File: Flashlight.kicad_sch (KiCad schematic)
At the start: 11 parts

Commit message: Finalized Kicad PCB Design
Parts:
- removed BT1: Battery_Cell, symbol Device:Battery_Cell
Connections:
- net 5V renamed 12V2
- net 12V2: no longer D1.2 (A), D10.2 (A), D7.2 (A), D8.2 (A), D9.2 (A)
- new net 12V1: D1.2 (A)
- new net 12V3: D10.2 (A), D7.2 (A), D8.2 (A), D9.2 (A)
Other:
- moved on the sheet: D1, D10, D2, D3, D4, D5, D6, D7, D8, D9

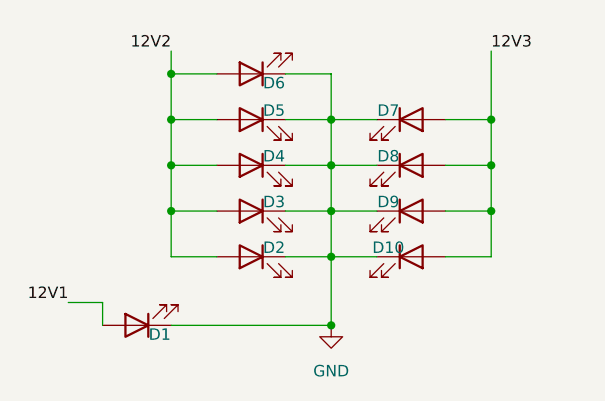
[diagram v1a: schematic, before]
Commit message: Made the PCB one Sided
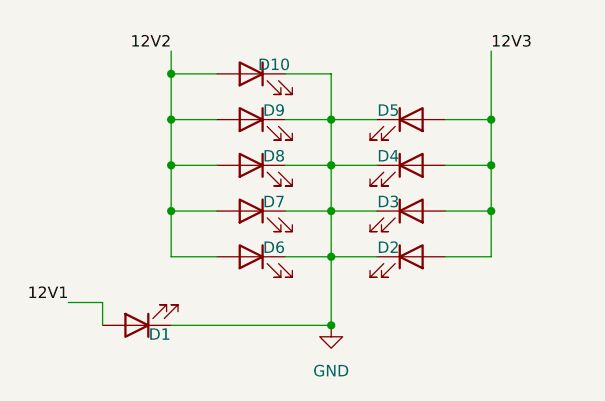
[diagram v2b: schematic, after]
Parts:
- renumbered D5 to D2, D6 to D3, D8 to D4, D7 to D5, D2 to D6, D3 to D7, D4 to D8
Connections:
- net 12V2: now also D10.2 (A), D9.2 (A); no longer D2.2 (A), D3.2 (A)
- net 12V3: now also D2.2 (A), D3.2 (A); no longer D10.2 (A), D9.2 (A)
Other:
- moved on the sheet: D10, D2, D3, D9
